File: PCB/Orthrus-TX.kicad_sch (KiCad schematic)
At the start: 135 parts, among them J1 HRO-TYPE-C-31-M-13x, U2 SRV05-4, U3 SRV05-4, U4 SRV05-4

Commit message: Update Orthrus-TX.kicad_sch
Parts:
- C1, C17, C29: LCSC C2177011 -> C19666
- POWER_1: LCSC (none) -> C293630
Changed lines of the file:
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@@
 			)
 		)
-		(property "LCSC" "C2177011"
+		(property "LCSC" "C19666"
 			(at 80.01 68.58 0)
 			(hide yes)
@@
 			)
 		)
-		(property "LCSC" "C2177011"
+		(property "LCSC" "C19666"
 			(at 138.43 68.58 0)
 			(hide yes)
@@
 			)
 		)
-		(property "LCSC" "C2177011"
+		(property "LCSC" "C19666"
 			(at 209.55 68.58 0)
 			(hide yes)
@@
 			(hide yes)
 			(show_name no)
+			(do_not_autoplace no)
+			(effects
+				(font
+					(size 1.27 1.27)
+				)
+			)
+		)
+		(property "LCSC" "C293630"
+			(at 147.32 41.91 90)
+			(hide yes)
+			(show_name no)

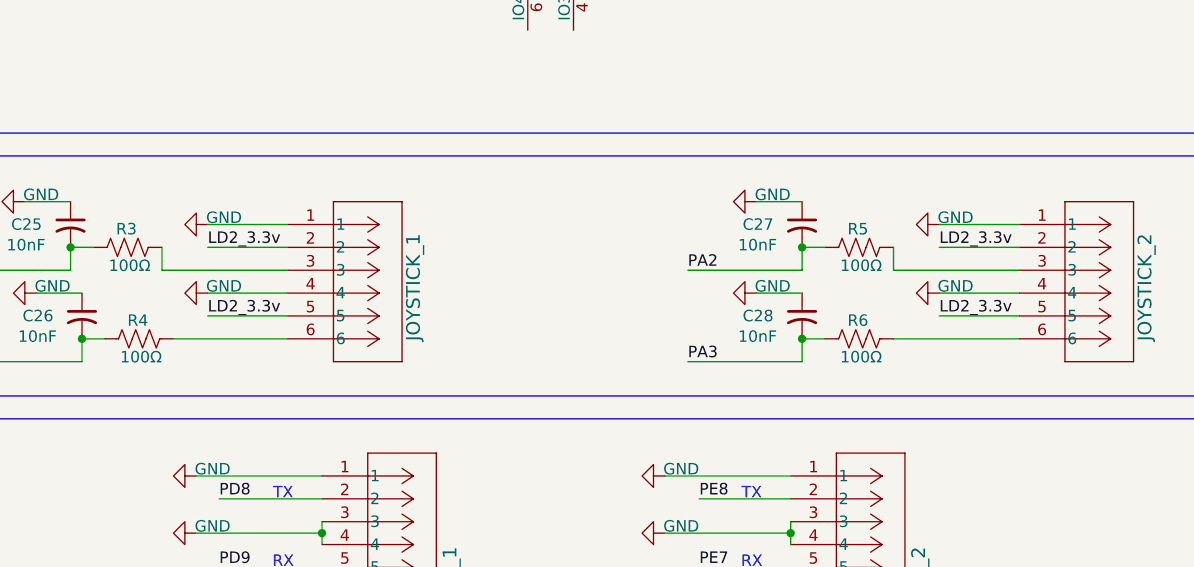
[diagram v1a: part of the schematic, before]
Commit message: change signal order for joysticks
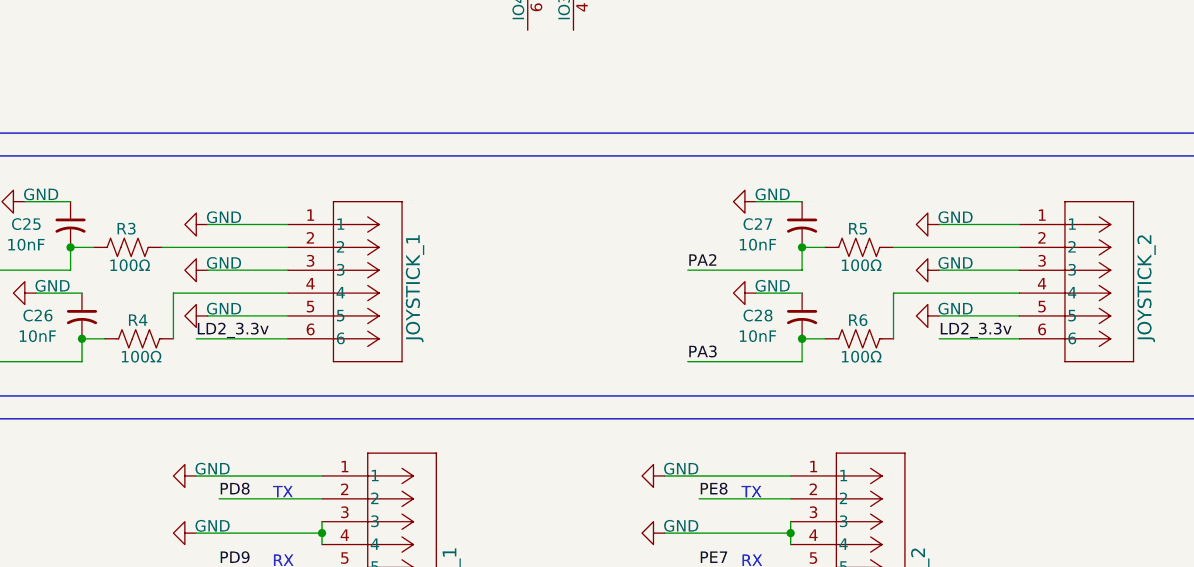
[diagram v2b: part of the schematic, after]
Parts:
- POWER_1: footprint CONN_532610001-SD_03_MOL -> Custom-Library:CONN_532610001-SD_03_MOL
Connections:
- net GND: now also JOYSTICK_1.3, JOYSTICK_1.5, JOYSTICK_2.3, JOYSTICK_2.5; no longer JOYSTICK_1.4, JOYSTICK_2.4
- net LD2_3.3v: now also JOYSTICK_1.6, JOYSTICK_2.6; no longer JOYSTICK_1.2, JOYSTICK_1.5, JOYSTICK_2.2, JOYSTICK_2.5
- net at R5.2: now also JOYSTICK_2.2; no longer JOYSTICK_2.3
- net at R3.2: now also JOYSTICK_1.2; no longer JOYSTICK_1.3
- net at R4.2: now also JOYSTICK_1.4; no longer JOYSTICK_1.6
- net at R6.2: now also JOYSTICK_2.4; no longer JOYSTICK_2.6

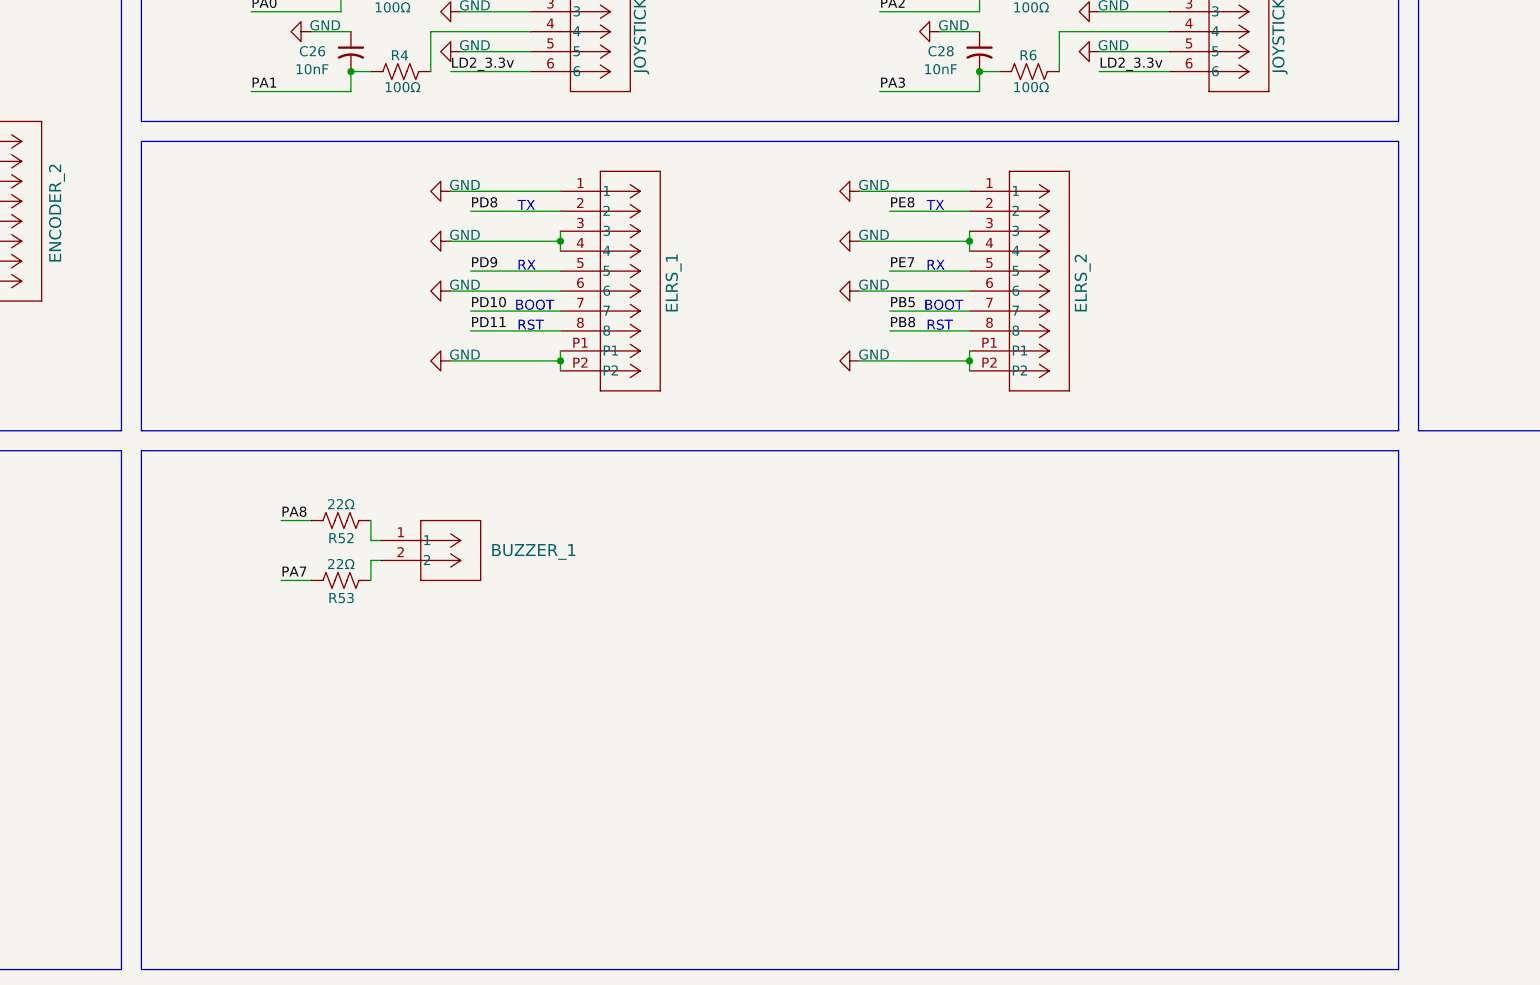
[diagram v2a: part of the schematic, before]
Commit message: add SRV05-4 for ELRS
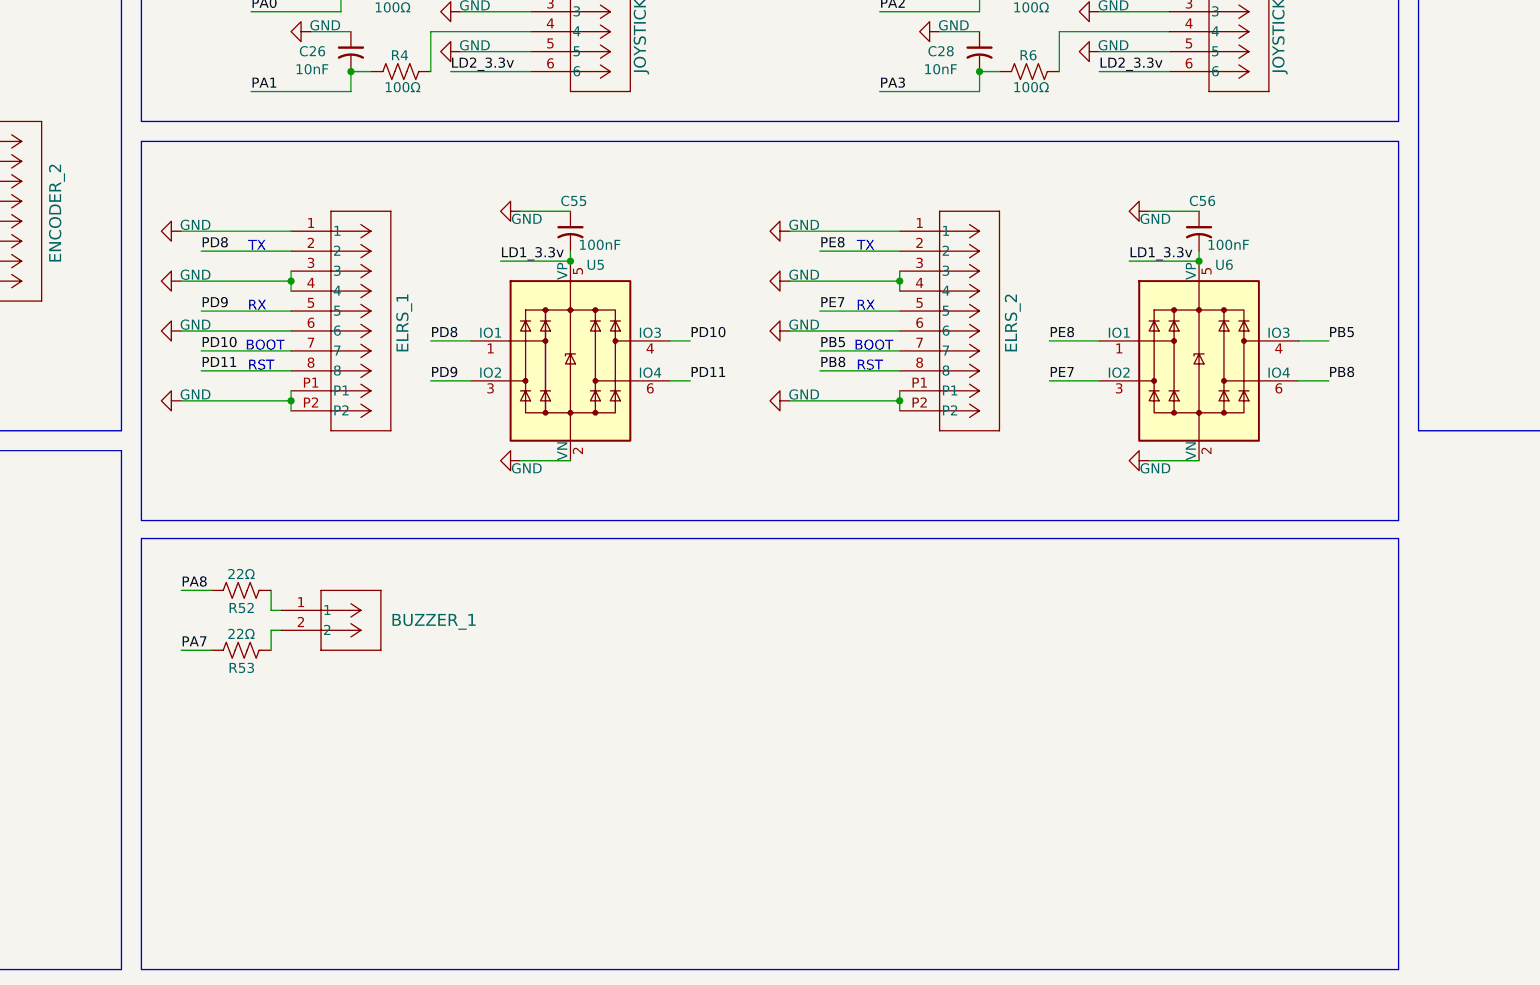
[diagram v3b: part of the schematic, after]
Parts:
- added C55, C56: 100nF, Capacitor_SMD:C_0603_1608Metric, symbol Device:C_Small_US
- added U5, U6: SRV05-4, Package_TO_SOT_SMD:SOT-23-6, symbol Power_Protection:SRV05-4
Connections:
- net GND: now also C55.1, C56.1, U5.2 (VN), U6.2 (VN)
- net LD1_3.3v: now also C55.2, C56.2, U5.5 (VP), U6.5 (VP)
- net PB5: now also U6.4 (IO3)
- net PB8: now also U6.6 (IO4)
- net PD10: now also U5.4 (IO3)
- net PD11: now also U5.6 (IO4)
- net PD8: now also U5.1 (IO1)
- net PD9: now also U5.3 (IO2)
- net PE7: now also U6.3 (IO2)
- net PE8: now also U6.1 (IO1)
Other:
- moved on the sheet: BUZZER_1, ELRS_1, ELRS_2, R52, R53

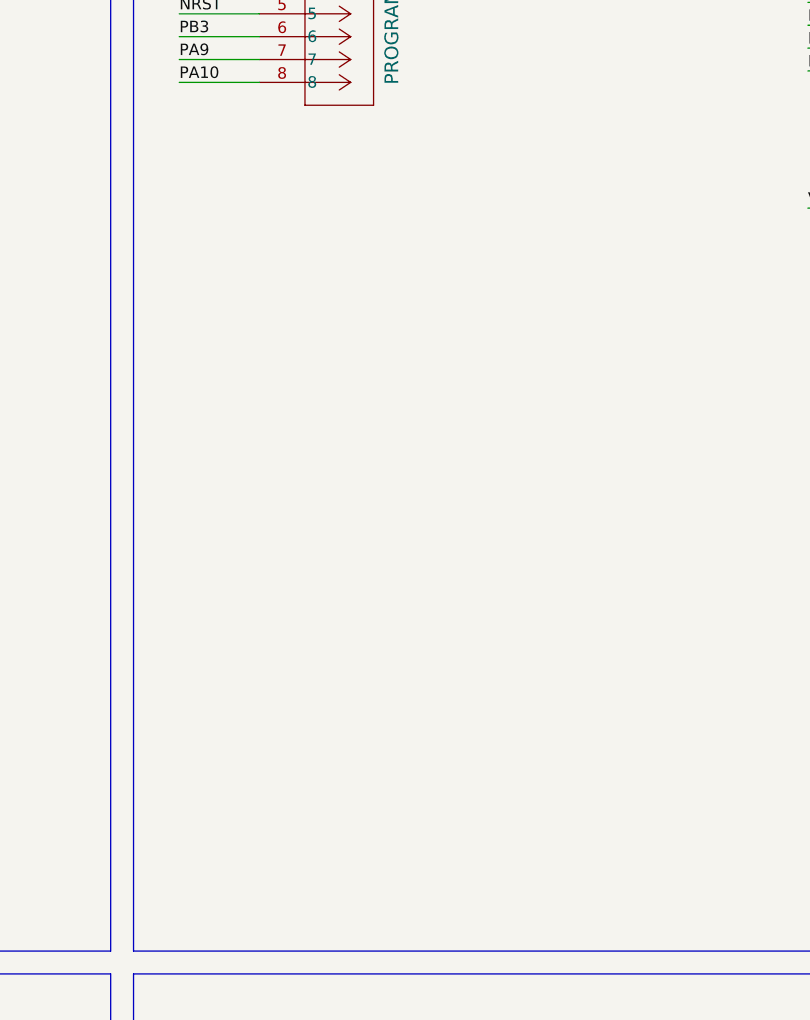
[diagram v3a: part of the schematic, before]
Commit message: add SRV05-4 for programming/debugging
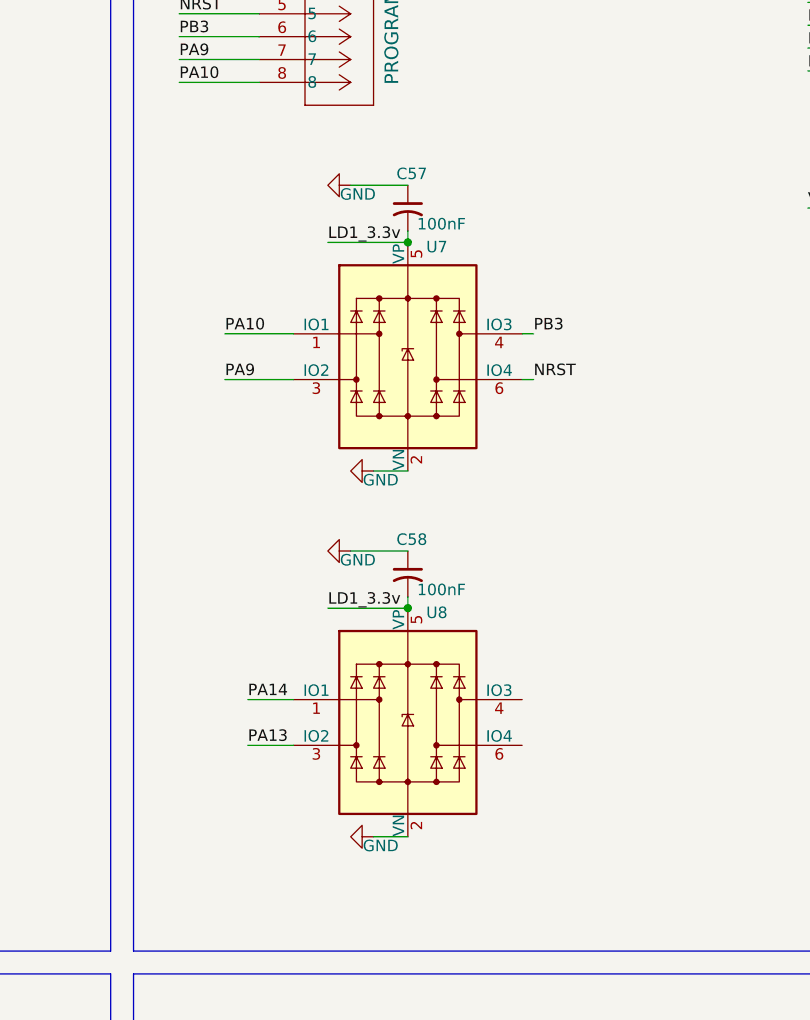
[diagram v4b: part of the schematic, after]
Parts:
- added C57, C58: 100nF, Capacitor_SMD:C_0603_1608Metric, symbol Device:C_Small_US
- added U7, U8: SRV05-4, Package_TO_SOT_SMD:SOT-23-6, symbol Power_Protection:SRV05-4
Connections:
- net GND: now also C57.1, C58.1, U7.2 (VN), U8.2 (VN)
- net LD1_3.3v: now also C57.2, C58.2, U7.5 (VP), U8.5 (VP)
- net NRST: now also U7.6 (IO4)
- net PA10: now also U7.1 (IO1)
- net PA13: now also U8.3 (IO2)
- net PA14: now also U8.1 (IO1)
- net PA9: now also U7.3 (IO2)
- net PB3: now also U7.4 (IO3)
